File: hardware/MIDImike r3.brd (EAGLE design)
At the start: 84.8 x 53.3 mm, 8 parts, among them SW1 PUSH-BTN, SW2 SH-7030TB

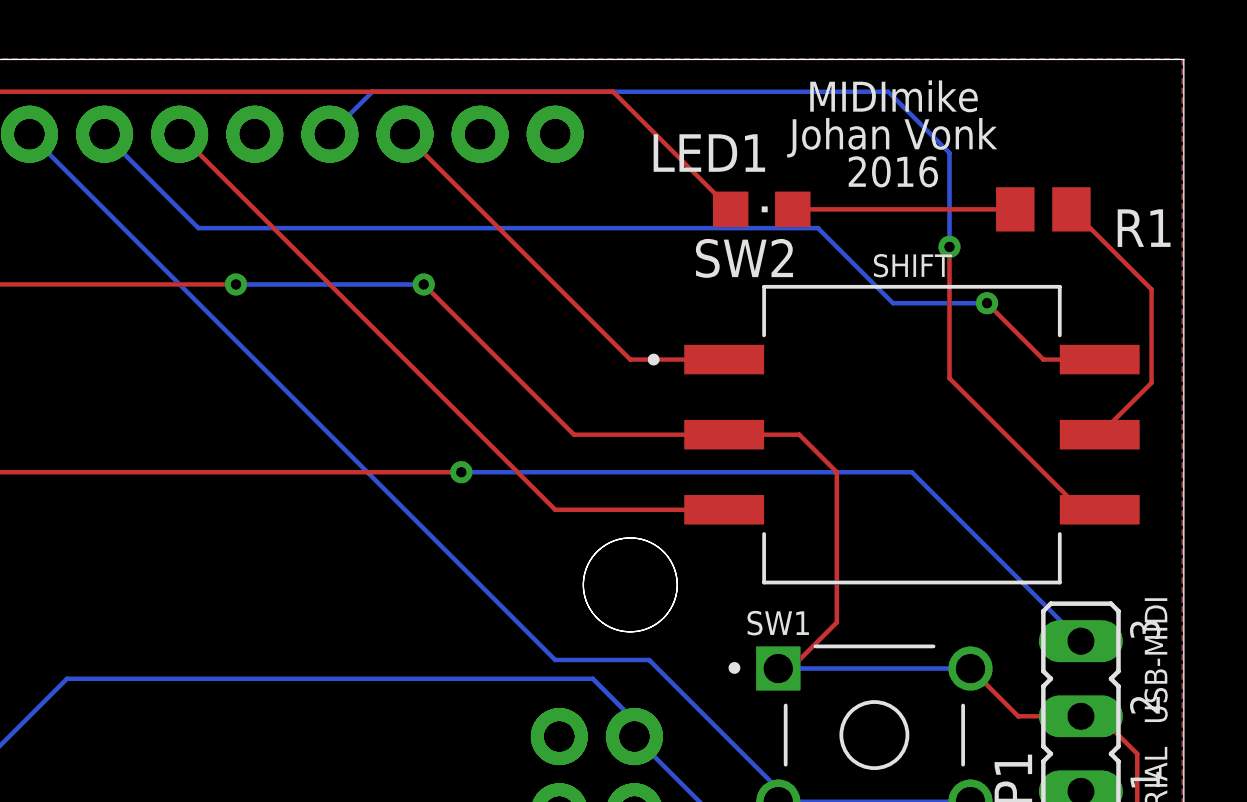
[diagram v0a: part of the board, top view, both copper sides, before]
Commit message: reduce footprint SW2
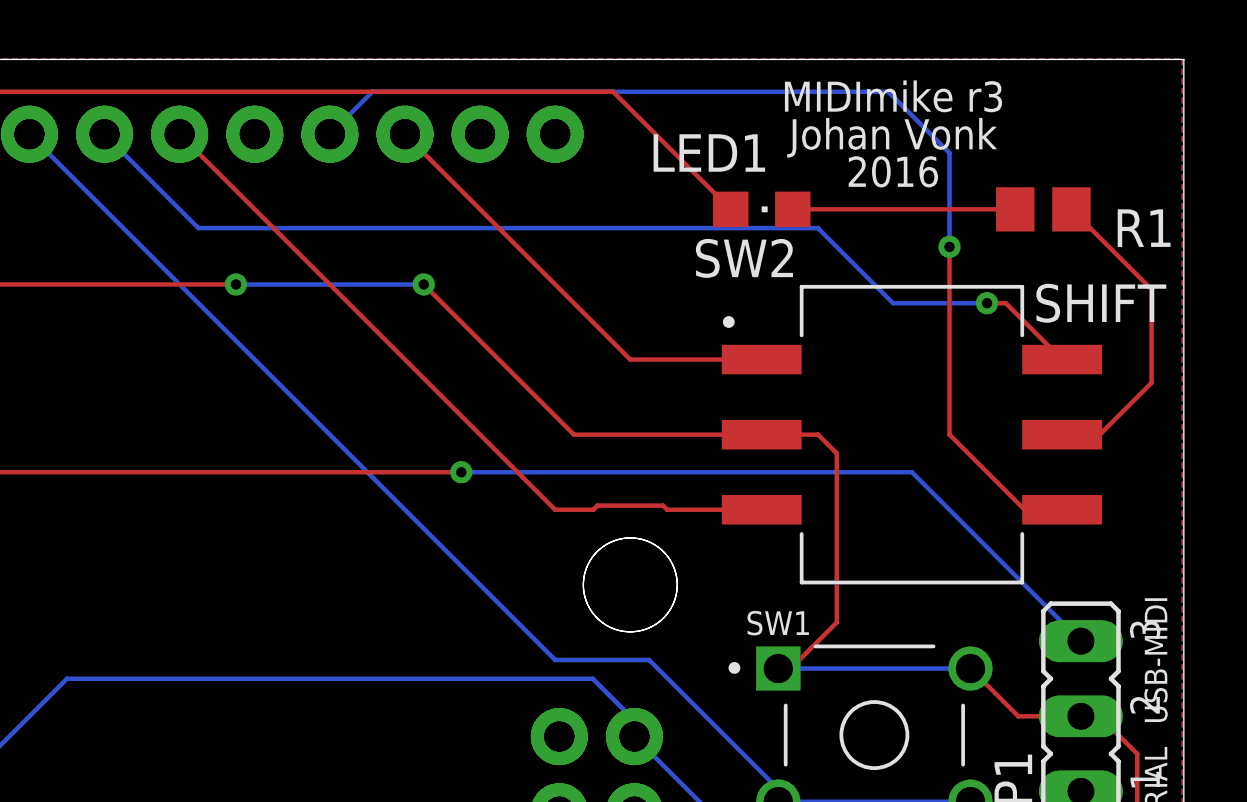
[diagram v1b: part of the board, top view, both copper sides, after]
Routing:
- net GND: track 185.9 -> 187.6 mm
- net N$13: track 23.7 -> 25.1 mm
- net N$14: track 36.8 -> 35.5 mm
- net N$1: track 14.0 -> 15.2 mm
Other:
- board text added: "MIDImike r3"
- board text removed: "MIDImike"
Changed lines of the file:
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@@
 <text x="83.82" y="33.02" size="0.762" layer="21" rot="R90" align="center">USB-MIDI</text>
 <text x="83.82" y="27.305" size="0.762" layer="21" rot="R90" align="center">USB-SERIAL</text>
-<text x="74.93" y="52.07" size="1.016" layer="21" align="center">MIDImike</text>
+<text x="74.93" y="52.07" size="1.016" layer="21" align="center">MIDImike r3</text>
 <text x="74.93" y="50.8" size="1.016" layer="21" align="center">Johan Vonk</text>
 <text x="74.93" y="49.53" size="1.016" layer="21" align="center">2016</text>
 <text x="53.34" y="25.4" size="2.032" layer="22" rot="MR0">https://github.com/jvonk/MIDImike</text>
-<text x="75.565" y="46.355" size="0.762" layer="21" rot="R180" align="center">SHIFT</text>
+<text x="81.915" y="45.085" size="1.27" layer="21" rot="R180" align="center">SHIFT</text>
 </plain>
 <attributes>
@@
 <wire x1="66.18000625" y1="25.3499875" x2="67.01899375" y2="24.511" width="0.1524" layer="1"/>
 <wire x1="67.01899375" y1="24.511" x2="71.3105" y2="24.511" width="0.1524" layer="1"/>
-<wire x1="69.215" y1="40.64" x2="71.755" y2="40.64" width="0.1524" layer="1"/>
-<wire x1="71.755" y1="40.64" x2="73.025" y2="39.37" width="0.1524" layer="1"/>
-<wire x1="73.025" y1="39.37" x2="73.025" y2="34.29" width="0.1524" layer="1"/>
 <wire x1="73.025" y1="34.29" x2="71.465" y2="32.73" width="0.1524" layer="1"/>
 <wire x1="71.465" y1="32.73" x2="71.045" y2="32.73" width="0.1524" layer="1"/>
-<wire x1="81.915" y1="40.64" x2="83.6678" y2="42.3928" width="0.1524" layer="1"/>
 <wire x1="83.6678" y1="45.5522" x2="80.96" y2="48.26" width="0.1524" layer="1"/>
 <wire x1="83.6678" y1="42.3928" x2="83.6678" y2="45.5522" width="0.1524" layer="1"/>
-<wire x1="69.215" y1="40.64" x2="64.135" y2="40.64" width="0.1524" layer="1"/>
 <wire x1="64.135" y1="40.64" x2="59.055" y2="45.72" width="0.1524" layer="1"/>
 <via x="59.055" y="45.72" extent="1-16" drill="0.35"/>
@@
 <wire x1="24.13" y1="43.815" x2="24.13" y2="48.26" width="0.1524" layer="1"/>
 <wire x1="24.13" y1="48.26" x2="26.67" y2="50.8" width="0.1524" layer="1"/>
+<wire x1="70.485" y1="40.64" x2="72.39" y2="40.64" width="0.1524" layer="1"/>
+<wire x1="72.39" y1="40.64" x2="73.025" y2="40.005" width="0.1524" layer="1"/>
+<wire x1="73.025" y1="40.005" x2="73.025" y2="34.29" width="0.1524" layer="1"/>
+<wire x1="70.485" y1="40.64" x2="64.135" y2="40.64" width="0.1524" layer="1"/>
+<wire x1="80.645" y1="40.64" x2="81.915" y2="40.64" width="0.1524" layer="1"/>
+<wire x1="81.915" y1="40.64" x2="83.6678" y2="42.3928" width="0.1524" layer="1"/>
 </signal>
 <signal name="5V">
@@
 <contactref element="PCB2" pad="D5"/>
 <contactref element="SW2" pad="4"/>
-<wire x1="50.8" y1="50.8" x2="63.5" y2="38.1" width="0.1524" layer="1"/>
-<wire x1="63.5" y1="38.1" x2="69.215" y2="38.1" width="0.1524" layer="1"/>
+<wire x1="63.5" y1="38.1" x2="50.8" y2="50.8" width="0.1524" layer="1"/>
+<wire x1="70.485" y1="38.1" x2="67.28966875" y2="38.1" width="0.1524" layer="1"/>
+<wire x1="67.28966875" y1="38.1" x2="67.14996875" y2="38.2397" width="0.1524" layer="1"/>
+<wire x1="67.14996875" y1="38.2397" x2="64.93003125" y2="38.2397" width="0.1524" layer="1"/>
+<wire x1="64.93003125" y1="38.2397" x2="64.79033125" y2="38.1" width="0.1524" layer="1"/>
+<wire x1="64.79033125" y1="38.1" x2="63.5" y2="38.1" width="0.1524" layer="1"/>
 </signal>
 <signal name="N$14">
 <contactref element="PCB2" pad="D6"/>
 <contactref element="SW2" pad="8"/>
-<wire x1="81.915" y1="43.18" x2="80.01" y2="43.18" width="0.1524" layer="1"/>
-<wire x1="80.01" y1="43.18" x2="78.105" y2="45.085" width="0.1524" layer="1"/>
 <via x="78.105" y="45.085" extent="1-16" drill="0.35"/>
 <wire x1="74.93" y1="45.085" x2="78.105" y2="45.085" width="0.1524" layer="16"/>
@@
 <wire x1="51.435" y1="47.625" x2="72.39" y2="47.625" width="0.1524" layer="16"/>
 <wire x1="72.39" y1="47.625" x2="74.93" y2="45.085" width="0.1524" layer="16"/>
+<wire x1="80.645" y1="43.18" x2="78.74" y2="45.085" width="0.1524" layer="1"/>
+<wire x1="78.74" y1="45.085" x2="78.105" y2="45.085" width="0.1524" layer="1"/>
 </signal>
 <signal name="D7">
@@
 <contactref element="PCB2" pad="D2"/>
 <contactref element="SW2" pad="1"/>
-<wire x1="58.42" y1="50.8" x2="66.04" y2="43.18" width="0.1524" layer="1"/>
-<wire x1="66.04" y1="43.18" x2="69.215" y2="43.18" width="0.1524" layer="1"/>
+<wire x1="66.04" y1="43.18" x2="58.42" y2="50.8" width="0.1524" layer="1"/>
+<wire x1="70.485" y1="43.18" x2="66.04" y2="43.18" width="0.1524" layer="1"/>
 </signal>
 <signal name="N$10">
 <contactref element="PCB2" pad="D3"/>
 <contactref element="SW2" pad="2"/>
-<wire x1="81.915" y1="38.1" x2="81.28" y2="38.1" width="0.1524" layer="1"/>
-<wire x1="81.28" y1="38.1" x2="76.835" y2="42.545" width="0.1524" layer="1"/>
+<wire x1="80.645" y1="38.1" x2="81.28" y2="38.1" width="0.1524" layer="1"/>
 <wire x1="76.835" y1="50.165" x2="74.7622" y2="52.2378" width="0.1524" layer="16"/>
 <wire x1="55.88" y1="50.8" x2="57.3178" y2="52.2378" width="0.1524" layer="16"/>
 <wire x1="57.3178" y1="52.2378" x2="74.7622" y2="52.2378" width="0.1524" layer="16"/>
-<wire x1="76.835" y1="42.545" x2="76.835" y2="46.99" width="0.1524" layer="1"/>
 <via x="76.835" y="46.99" extent="1-16" drill="0.35"/>
 <wire x1="76.835" y1="46.99" x2="76.835" y2="50.165" width="0.1524" layer="16"/>
+<wire x1="76.835" y1="40.64" x2="79.375" y2="38.1" width="0.1524" layer="1"/>
+<wire x1="76.835" y1="46.99" x2="76.835" y2="40.64" width="0.1524" layer="1"/>
+<wire x1="79.375" y1="38.1" x2="80.645" y2="38.1" width="0.1524" layer="1"/>
 </signal>
 <signal name="N$3">
